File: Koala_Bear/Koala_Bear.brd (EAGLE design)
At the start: 59.3 x 40 mm, 27 parts

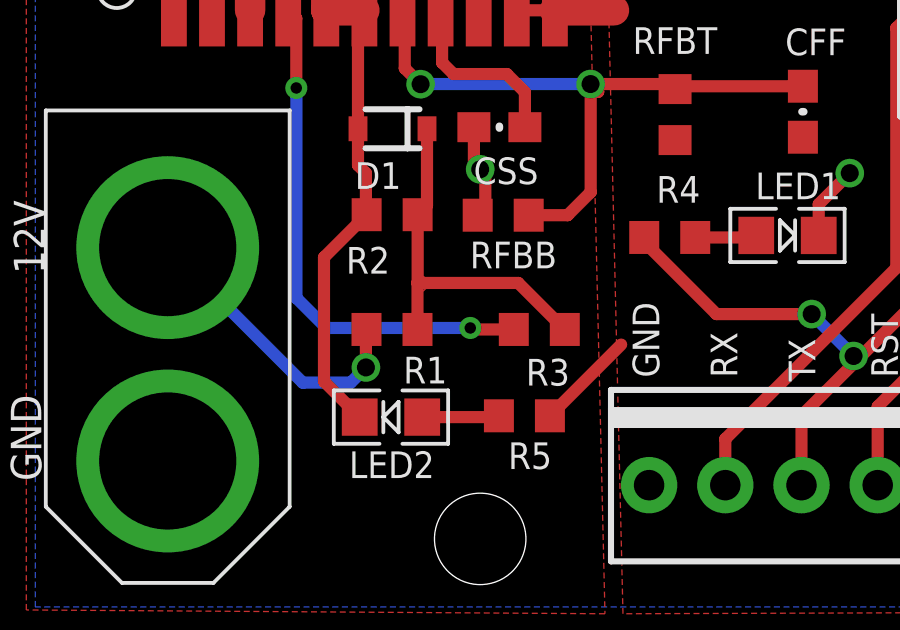
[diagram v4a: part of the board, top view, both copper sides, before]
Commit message: Further Review Fixes
1. Duly noted and changed
2. Hoping I removed the correct text
3. Basically, Doug used an oscilloscope today to demonstrate that
current was being sent through the serial line that we didn't have the
LED on. The TX/RX lines should be labeled wrt the Panda, thus why the
signal LED is now on the TX line.
4. Did I do this correctly? Looks like all the vias are now "tented."
5. Okidoke, got it.
6. It didn't have that in the value when it was first constructed, but I
went ahead and added it.
7. Consider them capitalized
8. Consider the value gone
9. I'll run it by Yip on Wednesday at worksession if I can catch him...
10. Glad it's clearer!
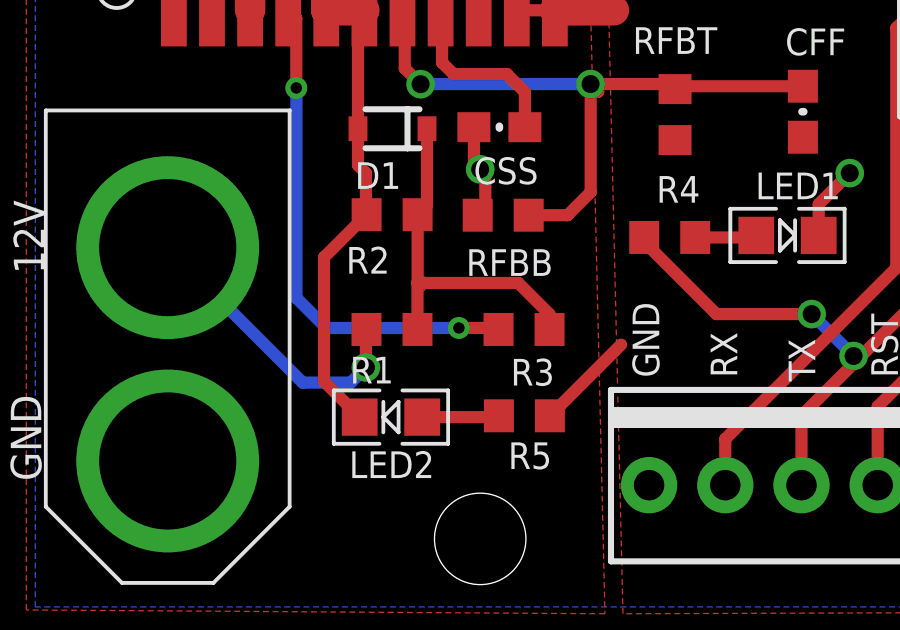
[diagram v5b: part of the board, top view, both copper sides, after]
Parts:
- CFF: value 4.7n -> 4.7nf
- moved R3 0.51 mm to (25.6, 12.9)
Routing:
- net EN: track 17.4 -> 16.9 mm
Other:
- board text added: ".47UF"
- board text added: "10UF"
- board text added: "4.7NF"
- board text added: "470UF"
- board text added: "47UF"
- board text added: "Copyright (c) 2013, Pioneers in Engineering All rights reserved. Designed by: K. Rakelly and A. Hild This design is open source hardware. 11/14/2013"
- board text removed: ".47uf"
- board text removed: "10uf"
- board text removed: "4.7n"
- board text removed: "470uf"
- board text removed: "47uf"
- board text removed: "5.1V"
- board text removed: "Copyright (c) 2013, Pioneers in Engineering All rights reserved. Designed by: K. Rakelly and A. Hild This design is open source hardware. 10/16/2013"
- board text removed: "Vin12, Vout6, Imax10"
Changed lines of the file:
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@@
 <layer number="38" name="bTest" color="7" fill="1" visible="no" active="yes"/>
 <layer number="39" name="tKeepout" color="4" fill="11" visible="yes" active="yes"/>
-<layer number="40" name="bKeepout" color="1" fill="11" visible="no" active="yes"/>
-<layer number="41" name="tRestrict" color="4" fill="10" visible="no" active="yes"/>
-<layer number="42" name="bRestrict" color="1" fill="10" visible="no" active="yes"/>
-<layer number="43" name="vRestrict" color="2" fill="10" visible="no" active="yes"/>
+<layer number="40" name="bKeepout" color="1" fill="11" visible="yes" active="yes"/>
+<layer number="41" name="tRestrict" color="4" fill="10" visible="yes" active="yes"/>
+<layer number="42" name="bRestrict" color="1" fill="10" visible="yes" active="yes"/>
+<layer number="43" name="vRestrict" color="2" fill="10" visible="yes" active="yes"/>
 <layer number="44" name="Drills" color="7" fill="1" visible="no" active="yes"/>
 <layer number="45" name="Holes" color="7" fill="1" visible="no" active="yes"/>
@@
 Buck Switching Regulator
 Version 2 : Revision B</text>
-<text x="32.03" y="23.03" size="1.016" layer="22" font="vector" ratio="15" rot="MR0">Vin12, Vout6, Imax10</text>
 <wire x1="67.244" y1="2.39" x2="7.9" y2="2.39" width="0" layer="20"/>
 <wire x1="39.13" y1="12.505" x2="39.13" y2="42.17291875" width="0.254" layer="25"/>
@@
 Designed by: K. Rakelly and A. Hild
 This design is open source hardware.
-10/16/2013</text>
+11/14/2013</text>
 <text x="12.889" y="3.873" size="1.016" layer="22" font="vector" ratio="15" rot="MR180">For more information, visit pioneers.berkeley.edu/opensource</text>
 <text x="19.304" y="11.938" size="0.889" layer="27" font="vector" ratio="20" rot="R90">60k</text>
-<text x="27.686" y="14.224" size="0.889" layer="27" font="vector" ratio="20" rot="R270">100</text>
+<text x="27.305" y="14.097" size="0.889" layer="27" font="vector" ratio="20" rot="R270">100</text>
 <text x="19.177" y="15.748" size="0.889" layer="27" font="vector" ratio="20" rot="R90">30k</text>
 <text x="27.686" y="14.732" size="0.889" layer="27" font="vector" ratio="20" rot="R90">2.37k</text>
 <text x="32.893" y="18.542" size="0.889" layer="27" font="vector" ratio="20" rot="R90">15.4k</text>
-<text x="29.718" y="31.877" size="0.889" layer="27" font="vector" ratio="20" rot="R90">47uf</text>
-<text x="37.084" y="19.05" size="0.889" layer="27" font="vector" ratio="20" rot="R90">4.7n</text>
-<text x="19.304" y="18.415" size="0.889" layer="27" font="vector" ratio="20" rot="R90">5.1V</text>
-<text x="27.432" y="18.669" size="0.889" layer="27" font="vector" ratio="20" rot="R90">.47uf</text>
-<text x="37.338" y="26.162" size="0.889" layer="27" font="vector" ratio="20" rot="R180">470uf</text>
-<text x="9.017" y="25.4" size="0.889" layer="27" font="vector" ratio="20" rot="R90">10uf</text>
+<text x="29.718" y="31.877" size="0.889" layer="27" font="vector" ratio="20" rot="R90">47UF</text>
+<text x="37.084" y="19.05" size="0.889" layer="27" font="vector" ratio="20" rot="R90">4.7NF</text>
+<text x="27.432" y="18.669" size="0.889" layer="27" font="vector" ratio="20" rot="R90">.47UF</text>
+<text x="37.338" y="26.162" size="0.889" layer="27" font="vector" ratio="20" rot="R180">470UF</text>
+<text x="9.017" y="25.4" size="0.889" layer="27" font="vector" ratio="20" rot="R90">10UF</text>
 </plain>
 <attributes>
@@
 </class>
 </classes>
-<designrules name="advancedcircuits-33each-pie">
+<designrules name="advancedcircuits-33each-pie *">
 <description language="de">&lt;b&gt;EAGLE Design Rules&lt;/b&gt;
 &lt;p&gt;
@@
 <param name="mlMinCreamFrame" value="3mil"/>
 <param name="mlMaxCreamFrame" value="5mil"/>
-<param name="mlViaStopLimit" value="0mil"/>
+<param name="mlViaStopLimit" value="24mil"/>
 <param name="srRoundness" value="0"/>
 <param name="srMinRoundness" value="0mil"/>
@@
 <element name="U$1" library="LMZ12010" package="LMZ12010" value="LMZ12010" x="20.27" y="33.19" smashed="yes"/>
 <element name="R1" library="pie" package="R0603" value="60k" x="21.19" y="12.95" smashed="yes" rot="R180">
-<attribute name="NAME" x="23.027359375" y="12.039359375" size="0.889" layer="25" font="vector" ratio="20" rot="R180"/>
+<attribute name="NAME" x="21.249359375" y="12.039359375" size="0.889" layer="25" font="vector" ratio="20" rot="R180"/>
 </element>
 <element name="R2" library="pie" package="R0603" value="30k" x="21.195" y="16.775" smashed="yes">
@@
 </element>
 <element name="RFBB" library="pie" package="R0603" value="2.37k" x="24.897" y="16.758" smashed="yes" rot="R180">
-<attribute name="NAME" x="26.686" y="15.877" size="0.889" layer="25" font="vector" ratio="20" rot="R180"/>
-</element>
-<element name="CFF" library="pie" package="0603-CAP" value="4.7n" x="34.8860875" y="20.207425" smashed="yes" rot="R90">
+<attribute name="NAME" x="26.559" y="15.623" size="0.889" layer="25" font="vector" ratio="20" rot="R180"/>
+</element>
+<element name="CFF" library="pie" package="0603-CAP" value="4.7nf" x="34.8860875" y="20.207425" smashed="yes" rot="R90">
 <attribute name="NAME" x="36.326575" y="22.9810875" size="0.889" layer="25" font="vector" ratio="20" rot="R180"/>
 </element>
@@
 <attribute name="NAME" x="32.786659375" y="26.146403125" size="0.889" layer="25" font="vector" ratio="20" rot="R180"/>
 </element>
-<element name="R3" library="pie" package="R0603" value="100" x="26.1" y="12.95" smashed="yes" rot="R180">
-<attribute name="NAME" x="27.116" y="11.969" size="0.889" layer="25" font="vector" ratio="20" rot="R180"/>
+<element name="R3" library="pie" package="R0603" value="100" x="25.592" y="12.95" smashed="yes" rot="R180">
+<attribute name="NAME" x="26.608" y="11.969" size="0.889" layer="25" font="vector" ratio="20" rot="R180"/>
 </element>
 <element name="MSTRO_PINS" library="pie_new" package="1X04-MTA" value="" x="33.57" y="7.76" smashed="yes">
@@
 <element name="R4" library="pie" package="R0603" value="330" x="30.44729375" y="16.016" smashed="yes" rot="R180">
 <attribute name="NAME" x="31.46329375" y="18.064" size="0.889" layer="25" font="vector" ratio="20" rot="R180"/>
-<attribute name="VALUE" x="28.843" y="15.01870625" size="0.889" layer="27" font="vector" ratio="20" rot="R90"/>
+<attribute name="VALUE" x="28.843" y="14.89170625" size="0.889" layer="27" font="vector" ratio="20" rot="R90"/>
 </element>
 <element name="R5" library="pie" package="R0603" value="330" x="25.604290625" y="10.071421875" smashed="yes">
@@
 <contactref element="R3" pad="1"/>
 <wire x1="22.04" y1="12.95" x2="22.04" y2="14.5" width="0.4064" layer="1"/>
-<wire x1="26.95" y1="12.95" x2="25.4" y2="14.5" width="0.4064" layer="1"/>
 <wire x1="25.4" y1="14.5" x2="22.04" y2="14.5" width="0.4064" layer="1"/>
 <wire x1="22.045" y1="16.775" x2="22.045" y2="14.505" width="0.4064" layer="1"/>
@@
 <vertex x="21.971" y="14.224"/>
 </polygon>
+<wire x1="25.4" y1="14.5" x2="26.442" y2="13.458" width="0.4064" layer="1"/>
+<wire x1="26.442" y1="13.458" x2="26.442" y2="12.95" width="0.4064" layer="1"/>
 </signal>
 <signal name="EN">
 <contactref element="R3" pad="2"/>
 <contactref element="U$1" pad="4"/>
-<wire x1="25.25" y1="12.95" x2="23.85" y2="12.95" width="0.4064" layer="1"/>
-<wire x1="23.85" y1="12.95" x2="23.8" y2="13" width="0.4064" layer="1"/>
-<via x="23.8" y="13" extent="1-16" drill="0.381"/>
-<wire x1="23.8" y1="13" x2="19" y2="13" width="0.4064" layer="16"/>
+<via x="23.419" y="13" extent="1-16" drill="0.381"/>
+<wire x1="23.419" y1="13" x2="19" y2="13" width="0.4064" layer="16"/>
 <wire x1="19" y1="13" x2="18" y2="14" width="0.4064" layer="16"/>
 <wire x1="18" y1="14" x2="18" y2="21" width="0.4064" layer="16"/>
@@
 <wire x1="18" y1="21" x2="18" y2="23.3188" width="0.4064" layer="1"/>
 <wire x1="18" y1="23.3188" x2="17.73" y2="23.5888" width="0.4064" layer="1"/>
+<wire x1="24.742" y1="12.95" x2="24.692" y2="13" width="0.4064" layer="1"/>
+<wire x1="24.692" y1="13" x2="23.419" y2="13" width="0.4064" layer="1"/>
 </signal>
 <signal name="N$6">

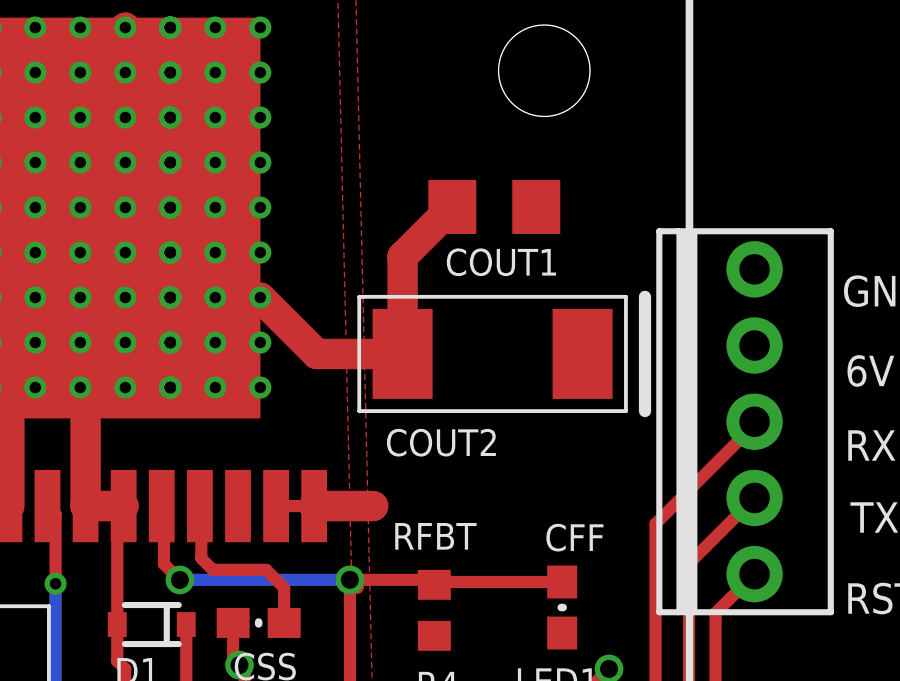
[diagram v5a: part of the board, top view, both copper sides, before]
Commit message: Goofs from last time now fixed
Change log:
1. Capitalization rules for capacitor values adhered to
2. COUT1 and COUT2 positions switched to facilitate easier
silkscreening.

This commit now reflects the board in an "as-is" state with none of the
changes that we might need for the TX/RX debate. What changes ought to
be made for that? Were further oscilloscope investigations performed to
confirm one hypothesis or another?
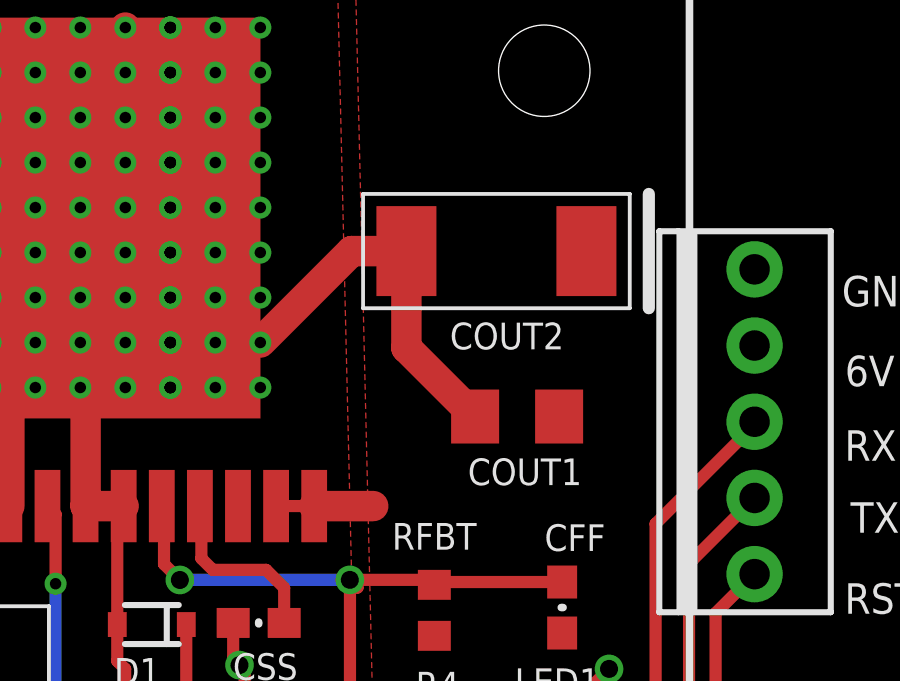
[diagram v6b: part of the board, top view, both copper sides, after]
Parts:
- moved COUT1 7.03 mm to (33.4, 26.6)
- moved COUT2 3.43 mm to (32.7, 32.1)
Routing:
- net GND: track 60.6 -> 62.1 mm
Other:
- board text added: ".47uF"
- board text added: "10uF"
- board text added: "4.7nF"
- board text added: "470uF"
- board text added: "47uF"
- board text added: "Copyright (c) 2013, Pioneers in Engineering All rights reserved. Designed by: K. Rakelly and A. Hild This design is open source hardware. 11/13/2013"
- board text removed: ".47UF"
- board text removed: "10UF"
- board text removed: "4.7NF"
- board text removed: "470UF"
- board text removed: "47UF"
- board text removed: "Copyright (c) 2013, Pioneers in Engineering All rights reserved. Designed by: K. Rakelly and A. Hild This design is open source hardware. 11/14/2013"
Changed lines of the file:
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@@
 Designed by: K. Rakelly and A. Hild
 This design is open source hardware.
-11/14/2013</text>
+11/13/2013</text>
 <text x="12.889" y="3.873" size="1.016" layer="22" font="vector" ratio="15" rot="MR180">For more information, visit pioneers.berkeley.edu/opensource</text>
 <text x="19.304" y="11.938" size="0.889" layer="27" font="vector" ratio="20" rot="R90">60k</text>
@@
 <text x="27.686" y="14.732" size="0.889" layer="27" font="vector" ratio="20" rot="R90">2.37k</text>
 <text x="32.893" y="18.542" size="0.889" layer="27" font="vector" ratio="20" rot="R90">15.4k</text>
-<text x="29.718" y="31.877" size="0.889" layer="27" font="vector" ratio="20" rot="R90">47UF</text>
-<text x="37.084" y="19.05" size="0.889" layer="27" font="vector" ratio="20" rot="R90">4.7NF</text>
-<text x="27.432" y="18.669" size="0.889" layer="27" font="vector" ratio="20" rot="R90">.47UF</text>
-<text x="37.338" y="26.162" size="0.889" layer="27" font="vector" ratio="20" rot="R180">470UF</text>
-<text x="9.017" y="25.4" size="0.889" layer="27" font="vector" ratio="20" rot="R90">10UF</text>
+<text x="30.48" y="25.019" size="0.889" layer="27" font="vector" ratio="20" rot="R90">47uF</text>
+<text x="37.084" y="19.05" size="0.889" layer="27" font="vector" ratio="20" rot="R90">4.7nF</text>
+<text x="27.432" y="18.669" size="0.889" layer="27" font="vector" ratio="20" rot="R90">.47uF</text>
+<text x="31.369" y="34.29" size="0.889" layer="27" font="vector" ratio="20">470uF</text>
+<text x="9.017" y="25.4" size="0.889" layer="27" font="vector" ratio="20" rot="R90">10uF</text>
 </plain>
 <attributes>
@@
 <attribute name="NAME" x="11.26" y="29.749" size="0.889" layer="25" font="vector" ratio="20" rot="R180"/>
 </element>
-<element name="COUT1" library="SparkFun" package="1206" value="47uF" x="32.622553125" y="33.557975" smashed="yes" rot="R180">
-<attribute name="NAME" x="34.781553125" y="32.160975" size="0.889" layer="25" font="vector" ratio="20" rot="R180"/>
+<element name="COUT1" library="SparkFun" package="1206" value="47uF" x="33.384553125" y="26.572975" smashed="yes" rot="R180">
+<attribute name="NAME" x="35.543553125" y="25.175975" size="0.889" layer="25" font="vector" ratio="20" rot="R180"/>
 </element>
 <element name="D1" library="SparkFun" package="SOD-323" value="5.1V" x="21.207" y="19.64" smashed="yes" rot="R180">
 <attribute name="NAME" x="21.496" y="18.524" size="0.889" layer="25" font="vector" ratio="20" rot="R180"/>
 </element>
-<element name="COUT2" library="TANT_CASE_E" package="TANT_CASE_E" value="470uF" x="32.567659375" y="28.659403125" smashed="yes" rot="R180">
-<attribute name="NAME" x="32.786659375" y="26.146403125" size="0.889" layer="25" font="vector" ratio="20" rot="R180"/>
+<element name="COUT2" library="TANT_CASE_E" package="TANT_CASE_E" value="470uF" x="32.694659375" y="32.088403125" smashed="yes" rot="R180">
+<attribute name="NAME" x="34.945659375" y="29.702403125" size="0.889" layer="25" font="vector" ratio="20" rot="R180"/>
 </element>
 <element name="R3" library="pie" package="R0603" value="100" x="25.592" y="12.95" smashed="yes" rot="R180">
@@
 <wire x1="24.301" y1="17.012" x2="24.301" y2="18.117" width="0.4064" layer="1"/>
 <wire x1="24.301" y1="18.117" x2="24.13" y2="18.288" width="0.4064" layer="1"/>
-<wire x1="31.222553125" y1="33.557975" x2="29.567659375" y2="31.90308125" width="1.016" layer="1"/>
-<wire x1="29.567659375" y1="31.90308125" x2="29.567659375" y2="28.659403125" width="1.016" layer="1"/>
-<wire x1="24.825" y1="30.54" x2="26.705596875" y2="28.659403125" width="1.016" layer="1"/>
-<wire x1="26.705596875" y1="28.659403125" x2="29.567659375" y2="28.659403125" width="1.016" layer="1"/>
+<wire x1="24.825" y1="29.04" x2="27.873403125" y2="32.088403125" width="1.016" layer="1"/>
+<wire x1="27.873403125" y1="32.088403125" x2="29.694659375" y2="32.088403125" width="1.016" layer="1"/>
+<wire x1="31.984553125" y1="26.572975" x2="29.694659375" y2="28.86286875" width="1.016" layer="1"/>
+<wire x1="29.694659375" y1="28.86286875" x2="29.694659375" y2="32.088403125" width="1.016" layer="1"/>
 </signal>
 <signal name="VOUT">
